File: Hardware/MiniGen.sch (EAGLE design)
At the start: 32 parts, among them U1 16MHz, U2 3.3V, U3 AD9837

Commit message: Added version info.
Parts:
- removed U$3: CREATIVE_COMMONS, SparkFun-Aesthetics:CREATIVE_COMMONS
- added FRAME1: FRAME-LETTER, SparkFun-Aesthetics:FRAME-LETTER
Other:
- note added: "03"
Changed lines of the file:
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@@
 <grid distance="0.1" unitdist="inch" unit="inch" style="lines" multiple="1" display="no" altdistance="0.01" altunitdist="inch" altunit="inch"/>
 <layers>
-<layer number="1" name="Top" color="4" fill="1" visible="yes" active="no"/>
-<layer number="2" name="Route2" color="1" fill="3" visible="yes" active="no"/>
-<layer number="3" name="Route3" color="4" fill="3" visible="yes" active="no"/>
-<layer number="4" name="Route4" color="1" fill="4" visible="yes" active="no"/>
-<layer number="5" name="Route5" color="4" fill="4" visible="yes" active="no"/>
-<layer number="6" name="Route6" color="1" fill="8" visible="yes" active="no"/>
-<layer number="7" name="Route7" color="4" fill="8" visible="yes" active="no"/>
-<layer number="8" name="Route8" color="1" fill="2" visible="yes" active="no"/>
-<layer number="9" name="Route9" color="4" fill="2" visible="yes" active="no"/>
-<layer number="10" name="Route10" color="1" fill="7" visible="yes" active="no"/>
-<layer number="11" name="Route11" color="4" fill="7" visible="yes" active="no"/>
-<layer number="12" name="Route12" color="1" fill="5" visible="yes" active="no"/>
-<layer number="13" name="Route13" color="4" fill="5" visible="yes" active="no"/>
-<layer number="14" name="Route14" color="1" fill="6" visible="yes" active="no"/>
-<layer number="15" name="Route15" color="4" fill="6" visible="yes" active="no"/>
-<layer number="16" name="Bottom" color="1" fill="1" visible="yes" active="no"/>
-<layer number="17" name="Pads" color="2" fill="1" visible="yes" active="no"/>
-<layer number="18" name="Vias" color="2" fill="1" visible="yes" active="no"/>
-<layer number="19" name="Unrouted" color="6" fill="1" visible="yes" active="no"/>
-<layer number="20" name="Dimension" color="15" fill="1" visible="yes" active="no"/>
-<layer number="21" name="tPlace" color="16" fill="1" visible="yes" active="no"/>
-<layer number="22" name="bPlace" color="14" fill="1" visible="yes" active="no"/>
-<layer number="23" name="tOrigins" color="15" fill="1" visible="yes" active="no"/>
-<layer number="24" name="bOrigins" color="15" fill="1" visible="yes" active="no"/>
-<layer number="25" name="tNames" color="7" fill="1" visible="yes" active="no"/>
-<layer number="26" name="bNames" color="7" fill="1" visible="yes" active="no"/>
-<layer number="27" name="tValues" color="7" fill="1" visible="yes" active="no"/>
-<layer number="28" name="bValues" color="7" fill="1" visible="yes" active="no"/>
+<layer number="1" name="Top" color="4" fill="1" visible="no" active="no"/>
+<layer number="2" name="Route2" color="1" fill="3" visible="no" active="no"/>
+<layer number="3" name="Route3" color="4" fill="3" visible="no" active="no"/>
+<layer number="4" name="Route4" color="1" fill="4" visible="no" active="no"/>
+<layer number="5" name="Route5" color="4" fill="4" visible="no" active="no"/>
+<layer number="6" name="Route6" color="1" fill="8" visible="no" active="no"/>
+<layer number="7" name="Route7" color="4" fill="8" visible="no" active="no"/>
+<layer number="8" name="Route8" color="1" fill="2" visible="no" active="no"/>
+<layer number="9" name="Route9" color="4" fill="2" visible="no" active="no"/>
+<layer number="10" name="Route10" color="1" fill="7" visible="no" active="no"/>
+<layer number="11" name="Route11" color="4" fill="7" visible="no" active="no"/>
+<layer number="12" name="Route12" color="1" fill="5" visible="no" active="no"/>
+<layer number="13" name="Route13" color="4" fill="5" visible="no" active="no"/>
+<layer number="14" name="Route14" color="1" fill="6" visible="no" active="no"/>
+<layer number="15" name="Route15" color="4" fill="6" visible="no" active="no"/>
+<layer number="16" name="Bottom" color="1" fill="1" visible="no" active="no"/>
+<layer number="17" name="Pads" color="2" fill="1" visible="no" active="no"/>
+<layer number="18" name="Vias" color="2" fill="1" visible="no" active="no"/>
+<layer number="19" name="Unrouted" color="6" fill="1" visible="no" active="no"/>
+<layer number="20" name="Dimension" color="15" fill="1" visible="no" active="no"/>
+<layer number="21" name="tPlace" color="16" fill="1" visible="no" active="no"/>
+<layer number="22" name="bPlace" color="14" fill="1" visible="no" active="no"/>
+<layer number="23" name="tOrigins" color="15" fill="1" visible="no" active="no"/>
+<layer number="24" name="bOrigins" color="15" fill="1" visible="no" active="no"/>
+<layer number="25" name="tNames" color="7" fill="1" visible="no" active="no"/>
+<layer number="26" name="bNames" color="7" fill="1" visible="no" active="no"/>
+<layer number="27" name="tValues" color="7" fill="1" visible="no" active="no"/>
+<layer number="28" name="bValues" color="7" fill="1" visible="no" active="no"/>
 <layer number="29" name="tStop" color="7" fill="3" visible="no" active="no"/>
 <layer number="30" name="bStop" color="7" fill="6" visible="no" active="no"/>
@@
 <layer number="35" name="tGlue" color="7" fill="4" visible="no" active="no"/>
 <layer number="36" name="bGlue" color="7" fill="5" visible="no" active="no"/>
-<layer number="37" name="tTest" color="7" fill="1" visible="yes" active="no"/>
-<layer number="38" name="bTest" color="7" fill="1" visible="yes" active="no"/>
+<layer number="37" name="tTest" color="7" fill="1" visible="no" active="no"/>
+<layer number="38" name="bTest" color="7" fill="1" visible="no" active="no"/>
 <layer number="39" name="tKeepout" color="4" fill="11" visible="no" active="no"/>
 <layer number="40" name="bKeepout" color="1" fill="11" visible="no" active="no"/>
@@
 <layer number="44" name="Drills" color="7" fill="1" visible="no" active="no"/>
 <layer number="45" name="Holes" color="7" fill="1" visible="no" active="no"/>
-<layer number="46" name="Milling" color="3" fill="1" visible="yes" active="no"/>
-<layer number="47" name="Measures" color="7" fill="1" visible="yes" active="no"/>
-<layer number="48" name="Document" color="7" fill="1" visible="yes" active="no"/>
-<layer number="49" name="Reference" color="7" fill="1" visible="yes" active="no"/>
-<layer number="50" name="dxf" color="7" fill="1" visible="yes" active="no"/>
-<layer number="51" name="tDocu" color="6" fill="1" visible="yes" active="no"/>
-<layer number="52" name="bDocu" color="7" fill="1" visible="yes" active="no"/>
-<layer number="53" name="tGND_GNDA" color="7" fill="9" visible="yes" active="no"/>
-<layer number="54" name="bGND_GNDA" color="1" fill="9" visible="yes" active="no"/>
-<layer number="56" name="wert" color="7" fill="1" visible="yes" active="no"/>
+<layer number="46" name="Milling" color="3" fill="1" visible="no" active="no"/>
+<layer number="47" name="Measures" color="7" fill="1" visible="no" active="no"/>
+<layer number="48" name="Document" color="7" fill="1" visible="no" active="no"/>
+<layer number="49" name="Reference" color="7" fill="1" visible="no" active="no"/>
+<layer number="50" name="dxf" color="7" fill="1" visible="no" active="no"/>
+<layer number="51" name="tDocu" color="6" fill="1" visible="no" active="no"/>
+<layer number="52" name="bDocu" color="7" fill="1" visible="no" active="no"/>
+<layer number="53" name="tGND_GNDA" color="7" fill="9" visible="no" active="no"/>
+<layer number="54" name="bGND_GNDA" color="1" fill="9" visible="no" active="no"/>
+<layer number="56" name="wert" color="7" fill="1" visible="no" active="no"/>
 <layer number="91" name="Nets" color="2" fill="1" visible="yes" active="yes"/>
 <layer number="92" name="Busses" color="1" fill="1" visible="yes" active="yes"/>
@@
 <part name="JP4" library="SparkFun-Aesthetics" deviceset="LOGO-SFE" device="NEW"/>
 <part name="U$2" library="SparkFun-Aesthetics" deviceset="OSHW-LOGO" device="S"/>
-<part name="U$3" library="SparkFun-Aesthetics" deviceset="CREATIVE_COMMONS" device=""/>
 <part name="U1" library="SparkFun-FreqCtrl" deviceset="OSCILLATOR" device="XTAL-11225" value="16MHz"/>
 <part name="GND2" library="SparkFun-Aesthetics" deviceset="GND" device=""/>
@@
 <text x="35.56" y="35.56" size="1.778" layer="95" font="vector">3.3V</text>
 <text x="50.8" y="106.68" size="1.778" layer="95" font="vector">3.3V-5V</text>
+<text x="238.506" y="6.35" size="3.81" layer="91">03</text>
 </plain>
 <instances>
@@
 <instance part="JP4" gate="G$1" x="241.3" y="17.78"/>
 <instance part="U$2" gate="G$1" x="236.22" y="45.72"/>
-<instance part="U$3" gate="G$1" x="66.04" y="2.54"/>
 <instance part="U1" gate="G$1" x="45.72" y="45.72"/>
 <instance part="GND2" gate="1" x="60.96" y="38.1" smashed="yes">

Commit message: Advance design to v10 for release.
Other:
- note added: "10"
- note removed: "03"
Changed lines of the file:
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@@
 <text x="35.56" y="35.56" size="1.778" layer="95" font="vector">3.3V</text>
 <text x="50.8" y="106.68" size="1.778" layer="95" font="vector">3.3V-5V</text>
-<text x="238.506" y="6.35" size="3.81" layer="91">03</text>
+<text x="238.506" y="6.35" size="3.81" layer="91">10</text>
 </plain>
 <instances>

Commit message: Fix labeling on schematic
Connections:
- net N$1 renamed OUT
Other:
- moved on the sheet: SJ1
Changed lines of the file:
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@@
 <part name="GND2" library="SparkFun-Aesthetics" deviceset="GND" device=""/>
 <part name="U4" library="SparkFun-AnalogIC" deviceset="ADC8045" device=""/>
+<part name="GND3" library="SparkFun-Aesthetics" deviceset="GND" device=""/>
+<part name="P+3" library="SparkFun-Aesthetics" deviceset="VCC" device="" value="VIN"/>
+<part name="P+4" library="SparkFun-Aesthetics" deviceset="VCC" device="" value="VIN"/>
+<part name="P+5" library="SparkFun-Aesthetics" deviceset="VCC" device=""/>
+<part name="P+6" library="SparkFun-Aesthetics" deviceset="VCC" device="" value="VIN"/>
 </parts>
 <sheets>
@@
 <attribute name="VALUE" x="93.98" y="93.98" size="1.778" layer="96" font="vector"/>
 </instance>
-<instance part="SJ1" gate="G$1" x="53.34" y="177.8" smashed="yes" rot="R90">
-<attribute name="NAME" x="51.054" y="179.705" size="1.778" layer="95" font="vector"/>
-<attribute name="VALUE" x="55.245" y="180.34" size="1.778" layer="96" rot="R90"/>
+<instance part="SJ1" gate="G$1" x="55.88" y="175.26" smashed="yes" rot="R90">
+<attribute name="NAME" x="53.594" y="177.165" size="1.778" layer="95" font="vector"/>
+<attribute name="VALUE" x="57.785" y="177.8" size="1.778" layer="96" rot="R90"/>
 </instance>
 <instance part="J1" gate="G$1" x="208.28" y="114.3" rot="R180"/>
@@
 </instance>
 <instance part="U4" gate="G$1" x="182.88" y="73.66"/>
+<instance part="GND3" gate="1" x="177.8" y="139.7" smashed="yes">
+<attribute name="VALUE" x="175.26" y="137.16" size="1.778" layer="96" font="vector"/>
+</instance>
+<instance part="P+3" gate="1" x="15.24" y="165.1" smashed="yes">
+<attribute name="VALUE" x="14.224" y="168.656" size="1.778" layer="96" font="vector"/>
+</instance>
+<instance part="P+4" gate="1" x="38.1" y="177.8" smashed="yes">
+<attribute name="VALUE" x="37.084" y="181.356" size="1.778" layer="96" font="vector"/>
+</instance>
+<instance part="P+5" gate="1" x="73.66" y="177.8" smashed="yes">
+<attribute name="VALUE" x="72.644" y="181.356" size="1.778" layer="96" font="vector"/>
+</instance>
+<instance part="P+6" gate="1" x="185.42" y="172.72" smashed="yes">
+<attribute name="VALUE" x="184.404" y="176.276" size="1.778" layer="96" font="vector"/>
+</instance>
 </instances>
 <busses>
@@
 </segment>
 <segment>
-<pinref part="JP3" gate="G$1" pin="2"/>
-<wire x1="193.04" y1="170.18" x2="182.88" y2="170.18" width="0.1524" layer="91"/>
-<label x="182.88" y="170.18" size="1.778" layer="95" font="vector"/>
-</segment>
-<segment>
 <pinref part="JP1" gate="G$1" pin="9"/>
 <wire x1="167.64" y1="165.1" x2="177.8" y2="165.1" width="0.1524" layer="91"/>
-<label x="172.72" y="165.1" size="1.778" layer="95" font="vector"/>
+<pinref part="GND3" gate="1" pin="GND"/>
+<wire x1="177.8" y1="165.1" x2="177.8" y2="142.24" width="0.1524" layer="91"/>
+<pinref part="JP3" gate="G$1" pin="2"/>
+<wire x1="193.04" y1="170.18" x2="177.8" y2="170.18" width="0.1524" layer="91"/>
+<wire x1="177.8" y1="170.18" x2="177.8" y2="165.1" width="0.1524" layer="91"/>
+<junction x="177.8" y="165.1"/>
 </segment>
 <segment>
@@
 <segment>
 <pinref part="SJ1" gate="G$1" pin="3"/>
-<wire x1="58.42" y1="177.8" x2="68.58" y2="177.8" width="0.1524" layer="91"/>
-<label x="63.5" y="177.8" size="1.778" layer="95" font="vector"/>
+<wire x1="60.96" y1="175.26" x2="73.66" y2="175.26" width="0.1524" layer="91"/>
+<pinref part="P+5" gate="1" pin="VCC"/>
+<wire x1="73.66" y1="175.26" x2="73.66" y2="177.8" width="0.1524" layer="91"/>
 </segment>
 <segment>
@@
 <net name="MCLK" class="0">
 <segment>
-<label x="55.88" y="76.2" size="1.778" layer="95" font="vector"/>
+<label x="58.42" y="48.26" size="1.778" layer="95" font="vector"/>
 <pinref part="U3" gate="G1" pin="MCLK"/>
 <wire x1="73.66" y1="48.26" x2="73.66" y2="76.2" width="0.1524" layer="91"/>
@@
 <pinref part="U3" gate="G1" pin="SCLK"/>
 <wire x1="25.4" y1="124.46" x2="45.72" y2="124.46" width="0.1524" layer="91"/>
-<label x="27.94" y="124.46" size="1.778" layer="95" font="vector"/>
+<label x="25.4" y="124.46" size="1.27" layer="95" font="vector" rot="R180" xref="yes"/>
 </segment>
 <segment>
 <pinref part="JP3" gate="G$1" pin="9"/>
-<wire x1="193.04" y1="152.4" x2="182.88" y2="152.4" width="0.1524" layer="91"/>
-<label x="182.88" y="152.4" size="1.778" layer="95" font="vector"/>
+<wire x1="193.04" y1="152.4" x2="190.5" y2="152.4" width="0.1524" layer="91"/>
+<label x="190.5" y="152.4" size="1.27" layer="95" font="vector" rot="R180" xref="yes"/>
 </segment>
 </net>
@@
 <pinref part="U3" gate="G1" pin="FSYNC"/>
 <wire x1="25.4" y1="119.38" x2="45.72" y2="119.38" width="0.1524" layer="91"/>
-<label x="27.94" y="119.38" size="1.778" layer="95" font="vector"/>
+<label x="25.4" y="119.38" size="1.27" layer="95" font="vector" rot="R180" xref="yes"/>
 </segment>
 <segment>
 <pinref part="JP3" gate="G$1" pin="12"/>
-<wire x1="193.04" y1="144.78" x2="182.88" y2="144.78" width="0.1524" layer="91"/>
+<wire x1="193.04" y1="144.78" x2="190.5" y2="144.78" width="0.1524" layer="91"/>
+<label x="190.5" y="144.78" size="1.27" layer="95" rot="R180" xref="yes"/>
 </segment>
 </net>
@@
 <pinref part="U3" gate="G1" pin="SDATA"/>
 <wire x1="25.4" y1="121.92" x2="45.72" y2="121.92" width="0.1524" layer="91"/>
-<label x="27.94" y="121.92" size="1.778" layer="95" font="vector"/>
+<label x="25.4" y="121.92" size="1.27" layer="95" font="vector" rot="R180" xref="yes"/>
 </segment>
 <segment>
 <pinref part="JP3" gate="G$1" pin="11"/>
-<wire x1="193.04" y1="147.32" x2="182.88" y2="147.32" width="0.1524" layer="91"/>
-<label x="182.88" y="147.32" size="1.778" layer="95" font="vector"/>
+<wire x1="193.04" y1="147.32" x2="190.5" y2="147.32" width="0.1524" layer="91"/>
+<label x="190.5" y="147.32" size="1.27" layer="95" font="vector" rot="R180" xref="yes"/>
 </segment>
 </net>
@@
 </segment>
 </net>
-<net name="N$1" class="0">
+<net name="OUT" class="0">
 <segment>
 <wire x1="200.66" y1="73.66" x2="200.66" y2="101.6" width="0.1524" layer="91"/>
@@
 <pinref part="U4" gate="G$1" pin="OUT"/>
 <wire x1="193.04" y1="73.66" x2="200.66" y2="73.66" width="0.1524" layer="91"/>
+<label x="193.04" y="73.66" size="1.778" layer="95"/>
+<label x="203.2" y="101.6" size="1.778" layer="95"/>
+<label x="200.66" y="114.3" size="1.778" layer="95"/>
 </segment>
 </net>
 <net name="VIN" class="0">
 <segment>
-<pinref part="JP3" gate="G$1" pin="4"/>
-<wire x1="193.04" y1="165.1" x2="182.88" y2="165.1" width="0.1524" layer="91"/>
-<label x="182.88" y="165.1" size="1.778" layer="95" font="vector"/>
-</segment>
-<segment>
-<pinref part="SJ1" gate="G$1" pin="2"/>
-<wire x1="53.34" y1="172.72" x2="53.34" y2="170.18" width="0.1524" layer="91"/>
-<wire x1="53.34" y1="170.18" x2="38.1" y2="170.18" width="0.1524" layer="91"/>
-<label x="38.1" y="170.18" size="1.778" layer="95" font="vector"/>
-</segment>
-<segment>
+<pinref part="P+3" gate="1" pin="VCC"/>
 <pinref part="U2" gate="G$1" pin="IN"/>
 <wire x1="43.18" y1="160.02" x2="40.64" y2="160.02" width="0.1524" layer="91"/>
@@
 <wire x1="40.64" y1="149.86" x2="40.64" y2="160.02" width="0.1524" layer="91"/>
 <junction x="40.64" y="160.02"/>
-<label x="20.32" y="160.02" size="1.778" layer="95" font="vector"/>
-</segment>
-<segment>
+<wire x1="15.24" y1="165.1" x2="15.24" y2="160.02" width="0.1524" layer="91"/>
+</segment>
+<segment>
+<pinref part="P+4" gate="1" pin="VCC"/>
+<wire x1="38.1" y1="177.8" x2="38.1" y2="175.26" width="0.1524" layer="91"/>
 <pinref part="SJ1" gate="G$1" pin="1"/>
-<wire x1="48.26" y1="177.8" x2="38.1" y2="177.8" width="0.1524" layer="91"/>
-<label x="38.1" y="177.8" size="1.778" layer="95" font="vector"/>
-</segment>
-</net>
+<wire x1="50.8" y1="175.26" x2="40.64" y2="175.26" width="0.1524" layer="91"/>
+<pinref part="SJ1" gate="G$1" pin="2"/>
+<wire x1="40.64" y1="175.26" x2="38.1" y2="175.26" width="0.1524" layer="91"/>
+<wire x1="55.88" y1="170.18" x2="55.88" y2="167.64" width="0.1524" layer="91"/>
+<wire x1="55.88" y1="167.64" x2="40.64" y2="167.64" width="0.1524" layer="91"/>
+<wire x1="40.64" y1="167.64" x2="40.64" y2="175.26" width="0.1524" layer="91"/>
+<junction x="40.64" y="175.26"/>
+</segment>
+<segment>
+<pinref part="P+6" gate="1" pin="VCC"/>
+<wire x1="185.42" y1="172.72" x2="185.42" y2="165.1" width="0.1524" layer="91"/>
+<pinref part="JP3" gate="G$1" pin="4"/>
+<wire x1="185.42" y1="165.1" x2="193.04" y2="165.1" width="0.1524" layer="91"/>
+</segment>
+</net>

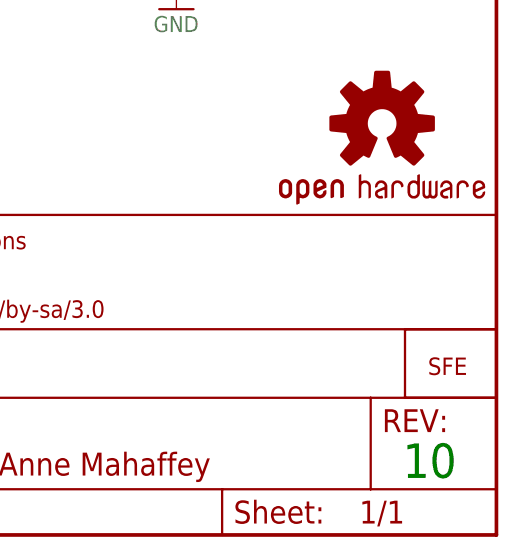
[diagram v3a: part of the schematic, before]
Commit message: added fiducials
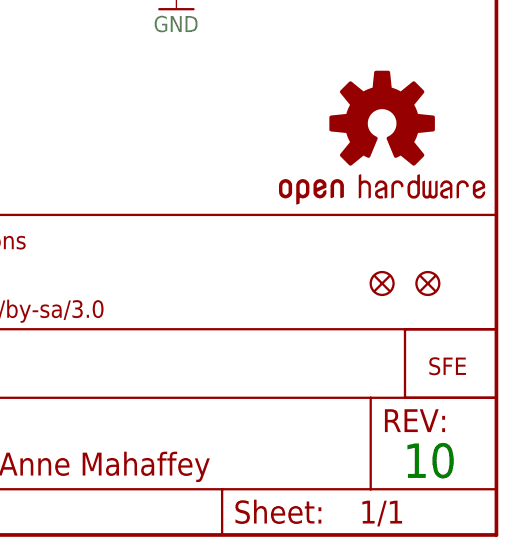
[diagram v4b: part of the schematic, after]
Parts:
- added FID1, FID2: FIDUCIAL1X2, SparkFun-Aesthetics:FIDUCIAL1X2
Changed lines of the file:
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@@
 <?xml version="1.0" encoding="utf-8"?>
 <!DOCTYPE eagle SYSTEM "eagle.dtd">
-<eagle version="6.4">
+<eagle version="6.5.0">
 <drawing>
 <settings>
@@
 <part name="P+5" library="SparkFun-Aesthetics" deviceset="VCC" device=""/>
 <part name="P+6" library="SparkFun-Aesthetics" deviceset="VCC" device="" value="VIN"/>
+<part name="FID1" library="SparkFun-Aesthetics" deviceset="FIDUCIAL" device="1X2"/>
+<part name="FID2" library="SparkFun-Aesthetics" deviceset="FIDUCIAL" device="1X2"/>
 </parts>
 <sheets>
@@
 <attribute name="VALUE" x="184.404" y="176.276" size="1.778" layer="96" font="vector"/>
 </instance>
+<instance part="FID1" gate="G$1" x="236.22" y="27.94"/>
+<instance part="FID2" gate="G$1" x="241.3" y="27.94"/>
 </instances>
 <busses>
